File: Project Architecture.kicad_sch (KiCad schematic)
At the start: 1 part

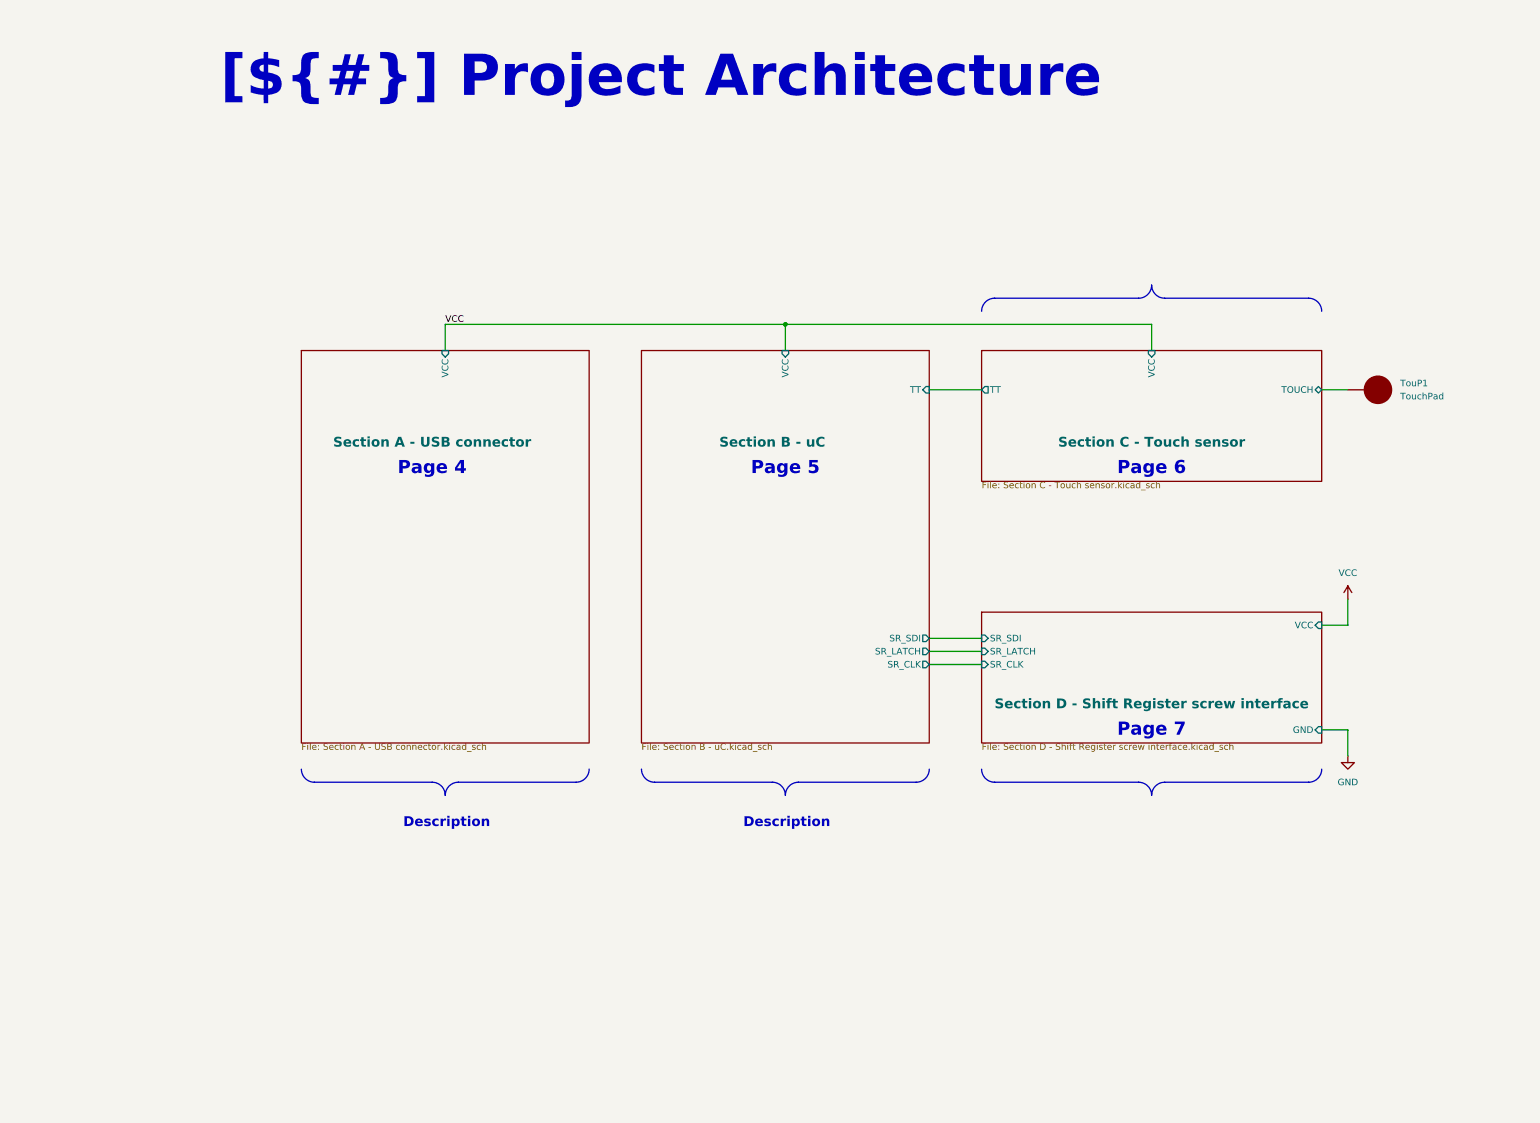
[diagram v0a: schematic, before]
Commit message: documentation update / block diagram
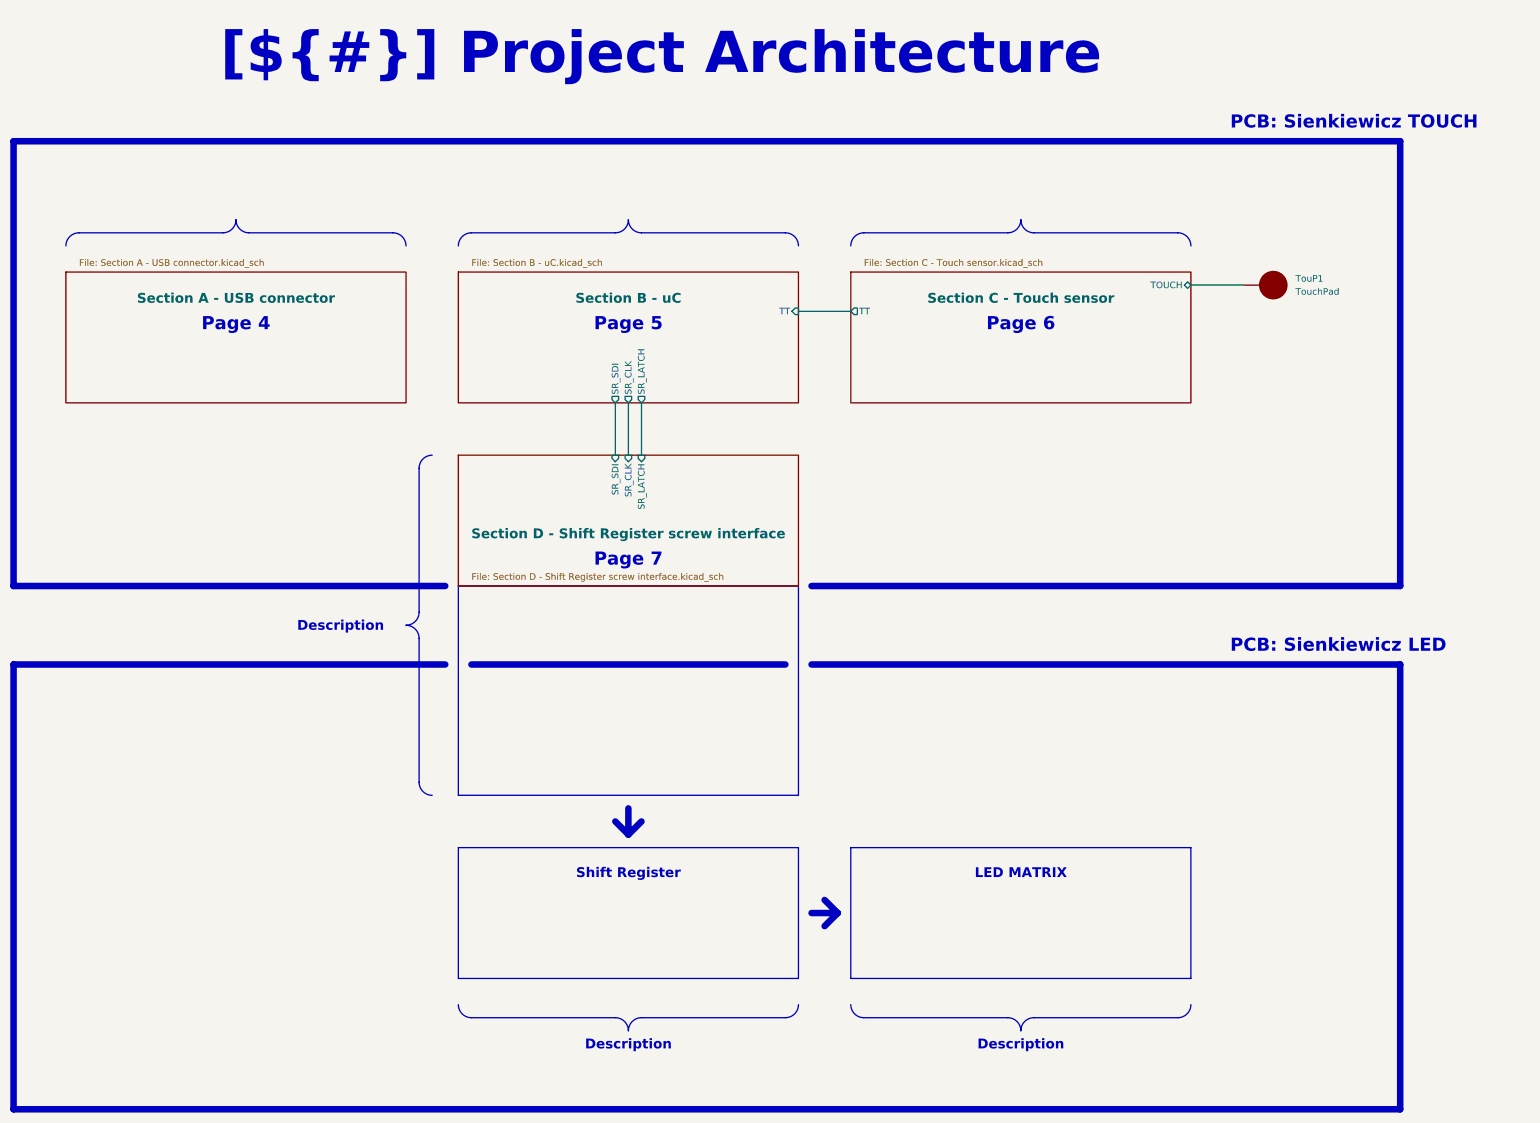
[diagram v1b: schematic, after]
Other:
- sheet Section A - USB connector ports: added none; removed VCC
- sheet Section B - uC ports: added none; removed VCC
- sheet Section C - Touch sensor ports: added none; removed VCC
- sheet Section D - Shift Register screw interface ports: added none; removed GND, VCC
- note added: "LED MATRIX"
- note added: "PCB: Sienkiewicz LED"
- note added: "PCB: Sienkiewicz TOUCH"
- note added: "Shift Register"
- moved on the sheet: TouP1

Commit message: routing update #4
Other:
- sheet Section B - uC ports: added SR_DAT; removed SR_SDI
- sheet Section D - Shift Register screw interface ports: added SR_DAT; removed SR_SDI
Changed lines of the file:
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@@
 			)
 		)
-		(pin "SR_SDI" input
+		(pin "SR_DAT" input
 			(at 200.66 101.6 90)
 			(effects
@@
 			)
 		)
-		(pin "SR_SDI" output
+		(pin "SR_DAT" output
 			(at 200.66 91.44 270)
 			(effects
